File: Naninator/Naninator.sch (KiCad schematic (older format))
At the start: 25 parts, among them J1 CONN_02X03, J101 USB_OTG, J2 CONN_01X15, J3 CONN_01X15, U001 FT232RL, U201 MAX8881, U401 ATMEGA328P-M, Y406 16MHz

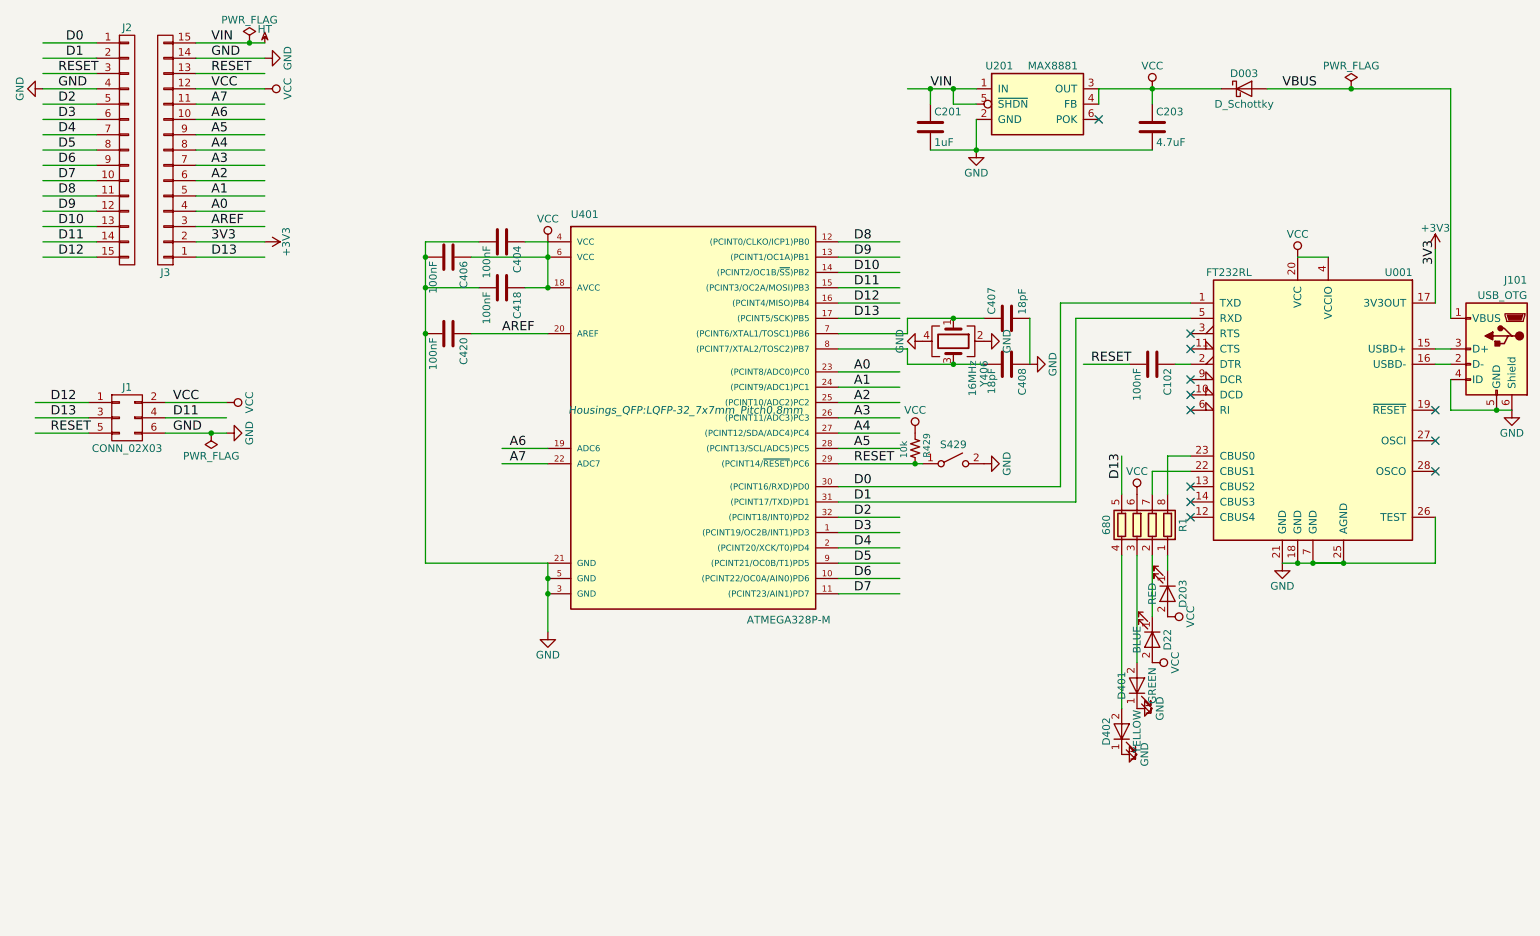
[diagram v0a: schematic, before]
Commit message: Routed the Naninator, except for two tracks
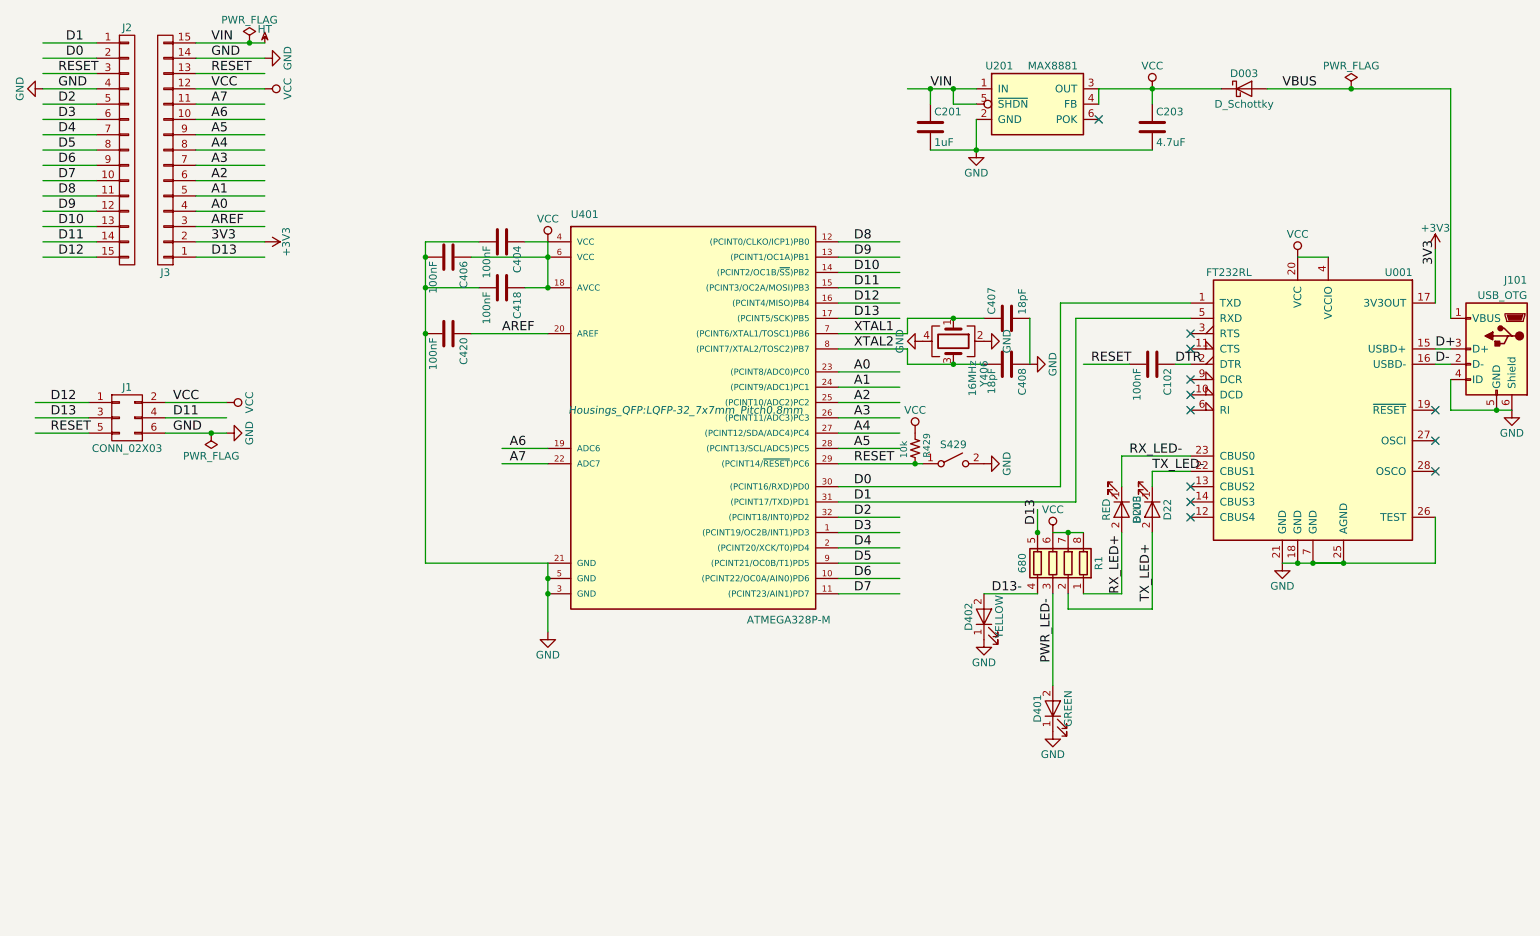
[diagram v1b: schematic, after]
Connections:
- net labels added: D+, D-, D13-, DTR, PWR_LED-, RX_LED+, RX_LED-, TX_LED+, TX_LED-, XTAL1, XTAL2
- wire segments 112 -> 116
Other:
- moved on the sheet: D203, D22, D401, D402, R1
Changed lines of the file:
@@
 $EndComp
+Wire Wire Line
+	1150 1050 800  1050
 Wire Wire Line
 	1150 950  800  950
 Wire Wire Line
-	1150 1050 800  1050
-Wire Wire Line
 	1150 1150 800  1150
 Wire Wire Line
 	1150 1250 800  1250
+Text Label 950  1050 0    60   ~ 0
+D0
 Text Label 950  950  0    60   ~ 0
-D0
-Text Label 950  1050 0    60   ~ 0
 D1
 Text Label 900  1150 0    60   ~ 0
@@
 L R_Pack04 R1
 U 1 1 58B740EE
-P 7950 4100
-F 0 "R1" V 7650 4100 50  0000 C CNN
-F 1 "680" V 8150 4100 50  0000 C CNN
-F 2 "Resistors_SMD:R_Array_Convex_4x0402" V 8225 4100 50  0001 C CNN
-F 3 "" H 7950 4100 50  0001 C CNN
-	1    7950 4100
+P 7400 4350
+F 0 "R1" V 7100 4350 50  0000 C CNN
+F 1 "680" V 7600 4350 50  0000 C CNN
+F 2 "Resistors_SMD:R_Array_Convex_4x0402" V 7675 4350 50  0001 C CNN
+F 3 "" H 7400 4350 50  0001 C CNN
+	1    7400 4350
 	-1   0    0    -1
 $EndComp
 Wire Wire Line
-	8300 3650 8150 3650
-Wire Wire Line
-	8150 3650 8150 3900
+	8300 3650 7850 3650
 Wire Wire Line
 	8300 3750 8050 3750
 Wire Wire Line
-	8050 3750 8050 3900
-Wire Wire Line
-	7850 3650 7850 3900
-Text Label 7850 3800 1    60   ~ 0
-D13
+	7300 4000 7300 4150
 $Comp
 L LED D203
 U 1 1 58B745FB
-P 8150 4550
-F 0 "D203" H 8150 4650 50  0000 C CNN
-F 1 "RED" H 8150 4450 50  0000 C CNN
-F 2 "LEDs:LED_0603" H 8150 4550 50  0001 C CNN
-F 3 "" H 8150 4550 50  0001 C CNN
-	1    8150 4550
+P 7850 4000
+F 0 "D203" H 7850 4100 50  0000 C CNN
+F 1 "RED" H 7850 3900 50  0000 C CNN
+F 2 "LEDs:LED_0603" H 7850 4000 50  0001 C CNN
+F 3 "" H 7850 4000 50  0001 C CNN
+	1    7850 4000
 	0    1    1    0
 $EndComp
@@
 L LED D22
 U 1 1 58B746B4
-P 8050 4850
-F 0 "D22" H 8050 4950 50  0000 C CNN
-F 1 "BLUE" H 8050 4750 50  0000 C CNN
-F 2 "LEDs:LED_0603" H 8050 4850 50  0001 C CNN
-F 3 "" H 8050 4850 50  0001 C CNN
-	1    8050 4850
+P 8050 4000
+F 0 "D22" H 8050 4100 50  0000 C CNN
+F 1 "BLUE" H 8050 3900 50  0000 C CNN
+F 2 "LEDs:LED_0603" H 8050 4000 50  0001 C CNN
+F 3 "" H 8050 4000 50  0001 C CNN
+	1    8050 4000
 	0    1    1    0
 $EndComp
@@
 L LED D401
 U 1 1 58B74705
-P 7950 5150
-F 0 "D401" H 7950 5250 50  0000 C CNN
-F 1 "GREEN" H 7950 5050 50  0000 C CNN
-F 2 "LEDs:LED_0603" H 7950 5150 50  0001 C CNN
-F 3 "" H 7950 5150 50  0001 C CNN
-	1    7950 5150
+P 7400 5300
+F 0 "D401" H 7400 5400 50  0000 C CNN
+F 1 "GREEN" H 7400 5200 50  0000 C CNN
+F 2 "LEDs:LED_0603" H 7400 5300 50  0001 C CNN
+F 3 "" H 7400 5300 50  0001 C CNN
+	1    7400 5300
 	0    -1   -1   0
 $EndComp
@@
 L LED D402
 U 1 1 58B74757
-P 7850 5450
-F 0 "D402" H 7850 5550 50  0000 C CNN
-F 1 "YELLOW" H 7850 5350 50  0000 C CNN
-F 2 "LEDs:LED_0603" H 7850 5450 50  0001 C CNN
-F 3 "" H 7850 5450 50  0001 C CNN
-	1    7850 5450
+P 6950 4700
+F 0 "D402" H 6950 4800 50  0000 C CNN
+F 1 "YELLOW" H 6950 4600 50  0000 C CNN
+F 2 "LEDs:LED_0603" H 6950 4700 50  0001 C CNN
+F 3 "" H 6950 4700 50  0001 C CNN
+	1    6950 4700
 	0    -1   -1   0
 $EndComp
 Wire Wire Line
-	8150 4400 8150 4300
-Wire Wire Line
-	8050 4700 8050 4300
-Wire Wire Line
-	7950 5000 7950 4300
-Wire Wire Line
-	7850 5300 7850 4300
+	7400 5150 7400 4550
+Wire Wire Line
+	6950 4550 7300 4550
 $Comp
 L VCC #PWR09
 U 1 1 58B74D0E
-P 7950 3900
-F 0 "#PWR09" H 7950 3750 50  0001 C CNN
-F 1 "VCC" H 7950 4050 50  0000 C CNN
-F 2 "" H 7950 3900 50  0001 C CNN
-F 3 "" H 7950 3900 50  0001 C CNN
-	1    7950 3900
-	1    0    0    -1
-$EndComp
-$Comp
-L VCC #PWR010
-U 1 1 58B74D48
-P 8150 4700
-F 0 "#PWR010" H 8150 4550 50  0001 C CNN
-F 1 "VCC" H 8150 4850 50  0000 C CNN
-F 2 "" H 8150 4700 50  0001 C CNN
-F 3 "" H 8150 4700 50  0001 C CNN
-	1    8150 4700
-	0    1    1    0
-$EndComp
-$Comp
-L VCC #PWR011
-U 1 1 58B74D82
-P 8050 5000
-F 0 "#PWR011" H 8050 4850 50  0001 C CNN
-F 1 "VCC" H 8050 5150 50  0000 C CNN
-F 2 "" H 8050 5000 50  0001 C CNN
-F 3 "" H 8050 5000 50  0001 C CNN
-	1    8050 5000
-	0    1    1    0
-$EndComp
-$Comp
-L GND #PWR012
+P 7400 4150
+F 0 "#PWR09" H 7400 4000 50  0001 C CNN
+F 1 "VCC" H 7400 4300 50  0000 C CNN
+F 2 "" H 7400 4150 50  0001 C CNN
+F 3 "" H 7400 4150 50  0001 C CNN
+	1    7400 4150
+	1    0    0    -1
+$EndComp
+$Comp
+L GND #PWR010
 U 1 1 58B74DBC
-P 7950 5300
-F 0 "#PWR012" H 7950 5050 50  0001 C CNN
-F 1 "GND" H 7950 5150 50  0000 C CNN
-F 2 "" H 7950 5300 50  0001 C CNN
-F 3 "" H 7950 5300 50  0001 C CNN
-	1    7950 5300
-	0    -1   -1   0
-$EndComp
-$Comp
-L GND #PWR013
+P 7400 5450
+F 0 "#PWR010" H 7400 5200 50  0001 C CNN
+F 1 "GND" H 7400 5300 50  0000 C CNN
+F 2 "" H 7400 5450 50  0001 C CNN
+F 3 "" H 7400 5450 50  0001 C CNN
+	1    7400 5450
+	1    0    0    -1
+$EndComp
+$Comp
+L GND #PWR011
 U 1 1 58B74DF6
-P 7850 5600
-F 0 "#PWR013" H 7850 5350 50  0001 C CNN
-F 1 "GND" H 7850 5450 50  0000 C CNN
-F 2 "" H 7850 5600 50  0001 C CNN
-F 3 "" H 7850 5600 50  0001 C CNN
-	1    7850 5600
-	0    -1   -1   0
+P 6950 4850
+F 0 "#PWR011" H 6950 4600 50  0001 C CNN
+F 1 "GND" H 6950 4700 50  0000 C CNN
+F 2 "" H 6950 4850 50  0001 C CNN
+F 3 "" H 6950 4850 50  0001 C CNN
+	1    6950 4850
+	1    0    0    -1
 $EndComp
 $Comp
@@
 $EndComp
 $Comp
-L HT #PWR014
+L HT #PWR012
 U 1 1 58B73E40
 P 2250 950
-F 0 "#PWR014" H 2250 1070 50  0001 C CNN
+F 0 "#PWR012" H 2250 1070 50  0001 C CNN
 F 1 "HT" H 2250 1040 50  0000 C CNN
 F 2 "" H 2250 950 50  0001 C CNN
@@
 Connection ~ 6750 1250
 $Comp
-L GND #PWR015
+L GND #PWR013
 U 1 1 58B74079
 P 6900 1650
-F 0 "#PWR015" H 6900 1400 50  0001 C CNN
+F 0 "#PWR013" H 6900 1400 50  0001 C CNN
 F 1 "GND" H 6900 1500 50  0000 C CNN
 F 2 "" H 6900 1650 50  0001 C CNN
@@
 3V3
 $Comp
-L +3V3 #PWR016
+L +3V3 #PWR014
 U 1 1 58B7578F
 P 9900 2300
-F 0 "#PWR016" H 9900 2150 50  0001 C CNN
+F 0 "#PWR014" H 9900 2150 50  0001 C CNN
 F 1 "+3V3" H 9900 2440 50  0000 C CNN
 F 2 "" H 9900 2300 50  0001 C CNN
@@
 $EndComp
 $Comp
-L GND #PWR017
+L GND #PWR015
 U 1 1 58B75EDB
 P 10400 3350
-F 0 "#PWR017" H 10400 3100 50  0001 C CNN
+F 0 "#PWR015" H 10400 3100 50  0001 C CNN
 F 1 "GND" H 10400 3200 50  0000 C CNN
 F 2 "" H 10400 3350 50  0001 C CNN
@@
 $EndComp
 $Comp
-L +3V3 #PWR018
+L +3V3 #PWR016
 U 1 1 58B75F1F
 P 2250 2250
-F 0 "#PWR018" H 2250 2100 50  0001 C CNN
+F 0 "#PWR016" H 2250 2100 50  0001 C CNN
 F 1 "+3V3" H 2250 2390 50  0000 C CNN
 F 2 "" H 2250 2250 50  0001 C CNN
@@
 $EndComp
 $Comp
-L VCC #PWR019
+L VCC #PWR017
 U 1 1 58B75F63
 P 9000 2350
-F 0 "#PWR019" H 9000 2200 50  0001 C CNN
+F 0 "#PWR017" H 9000 2200 50  0001 C CNN
 F 1 "VCC" H 9000 2500 50  0000 C CNN
 F 2 "" H 9000 2350 50  0001 C CNN
@@
 Connection ~ 9100 4350
 $Comp
-L GND #PWR020
+L GND #PWR018
 U 1 1 58B76440
 P 8900 4350
-F 0 "#PWR020" H 8900 4100 50  0001 C CNN
+F 0 "#PWR018" H 8900 4100 50  0001 C CNN
 F 1 "GND" H 8900 4200 50  0000 C CNN
 F 2 "" H 8900 4350 50  0001 C CNN
@@
 NoConn ~ 7700 1450
 $Comp
-L PWR_FLAG #FLG021
+L PWR_FLAG #FLG019
 U 1 1 58B8A8A6
 P 2150 950
-F 0 "#FLG021" H 2150 1025 50  0001 C CNN
+F 0 "#FLG019" H 2150 1025 50  0001 C CNN
 F 1 "PWR_FLAG" H 2150 1100 50  0000 C CNN
 F 2 "" H 2150 950 50  0001 C CNN
@@
 $EndComp
 $Comp
-L PWR_FLAG #FLG022
+L PWR_FLAG #FLG020
 U 1 1 58B8A8E8
 P 1900 3500
-F 0 "#FLG022" H 1900 3575 50  0001 C CNN
+F 0 "#FLG020" H 1900 3575 50  0001 C CNN
 F 1 "PWR_FLAG" H 1900 3650 50  0000 C CNN
 F 2 "" H 1900 3500 50  0001 C CNN
@@
 $EndComp
 $Comp
-L VCC #PWR023
+L VCC #PWR021
 U 1 1 58B8B4A6
 P 8050 1250
-F 0 "#PWR023" H 8050 1100 50  0001 C CNN
+F 0 "#PWR021" H 8050 1100 50  0001 C CNN
 F 1 "VCC" H 8050 1400 50  0000 C CNN
 F 2 "" H 8050 1250 50  0001 C CNN
@@
 Connection ~ 2150 950
 $Comp
-L GND #PWR024
+L GND #PWR022
 U 1 1 58B8C7FC
 P 6950 3700
-F 0 "#PWR024" H 6950 3450 50  0001 C CNN
+F 0 "#PWR022" H 6950 3450 50  0001 C CNN
 F 1 "GND" H 6950 3550 50  0000 C CNN
 F 2 "" H 6950 3700 50  0001 C CNN
@@
 Connection ~ 6500 3700
 $Comp
-L VCC #PWR025
+L VCC #PWR023
 U 1 1 58B8D268
 P 6500 3500
-F 0 "#PWR025" H 6500 3350 50  0001 C CNN
+F 0 "#PWR023" H 6500 3350 50  0001 C CNN
 F 1 "VCC" H 6500 3650 50  0000 C CNN
 F 2 "" H 6500 3500 50  0001 C CNN
@@
 VBUS
 $Comp
-L PWR_FLAG #FLG026
+L PWR_FLAG #FLG024
 U 1 1 58B8D917
 P 9350 1250
-F 0 "#FLG026" H 9350 1325 50  0001 C CNN
+F 0 "#FLG024" H 9350 1325 50  0001 C CNN
 F 1 "PWR_FLAG" H 9350 1400 50  0000 C CNN
 F 2 "" H 9350 1250 50  0001 C CNN
@@
 $EndComp
 $Comp
-L GND #PWR027
+L GND #PWR025
 U 1 1 58BA02E7
 P 6950 2900
-F 0 "#PWR027" H 6950 2650 50  0001 C CNN
+F 0 "#PWR025" H 6950 2650 50  0001 C CNN
 F 1 "GND" H 6950 2750 50  0000 C CNN
 F 2 "" H 6950 2900 50  0001 C CNN
@@
 	0    -1   -1   0
 $EndComp
-$Comp
-L GND #PWR028
-U 1 1 58BA032D
+Wire Wire Line
+	7850 3650 7850 3850
+Wire Wire Line
+	8050 3750 8050 3850
+Wire Wire Line
+	7400 4150 7600 4150
+Wire Wire Line
+	8050 4150 8050 4650
+Wire Wire Line
+	8050 4650 7500 4650
+Wire Wire Line
+	7500 4650 7500 4550
+Wire Wire Line
+	7850 4150 7850 4550
+Wire Wire Line
+	7850 4550 7600 4550
+Text Label 7300 4100 1    60   ~ 0
+D13
+Connection ~ 7300 4150
+Text Label 9900 2950 0    60   ~ 0
+D+
+Text Label 9900 3050 0    60   ~ 0
+D-
+Text Label 7900 3650 0    60   ~ 0
+RX_LED-
+Text Label 8050 3750 0    60   ~ 0
+TX_LED-
+Text Label 7850 4550 1    60   ~ 0
+RX_LED+
+Text Label 8050 4600 1    60   ~ 0
+TX_LED+
+Text Label 8200 3050 0    60   ~ 0
+DTR
+Text Label 6100 2850 0    60   ~ 0
+XTAL1
+Text Label 6100 2950 0    60   ~ 0
+XTAL2
+Connection ~ 7500 4150
+Text Label 7000 4550 0    60   ~ 0
+D13-
+Text Label 7400 5000 1    60   ~ 0
+PWR_LED-
+$Comp
+L GND #PWR?
+U 1 1 58BC5FE1
 P 6550 2900
-F 0 "#PWR028" H 6550 2650 50  0001 C CNN
+F 0 "#PWR?" H 6550 2650 50  0001 C CNN
 F 1 "GND" H 6550 2750 50  0000 C CNN
 F 2 "" H 6550 2900 50  0001 C CNN

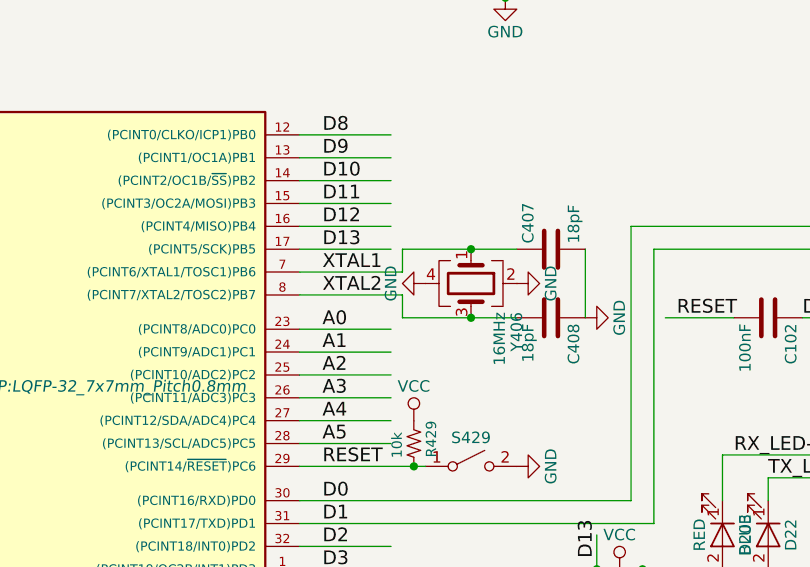
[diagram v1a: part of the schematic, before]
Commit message: One or two ground connections are left
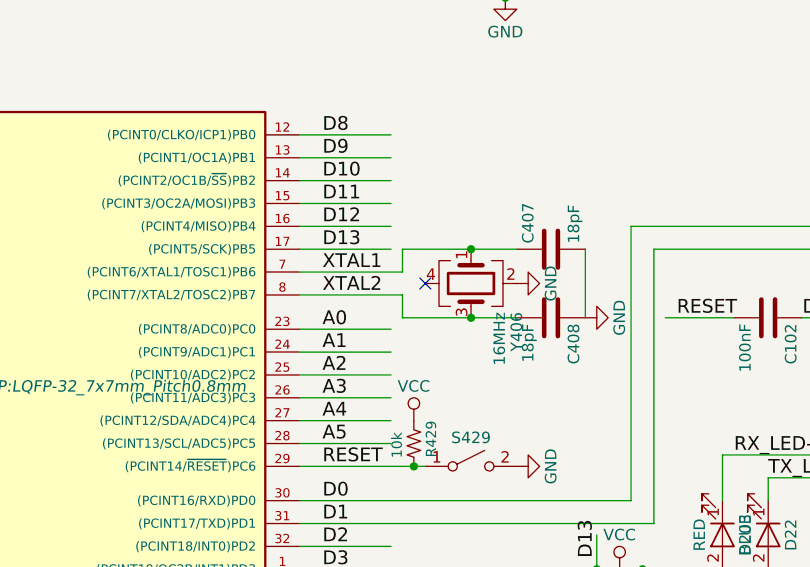
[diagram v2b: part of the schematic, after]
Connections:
- no-connect marks 12 -> 13
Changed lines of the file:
@@
 Text Label 7400 5000 1    60   ~ 0
 PWR_LED-
-$Comp
-L GND #PWR?
-U 1 1 58BC5FE1
-P 6550 2900
-F 0 "#PWR?" H 6550 2650 50  0001 C CNN
-F 1 "GND" H 6550 2750 50  0000 C CNN
-F 2 "" H 6550 2900 50  0001 C CNN
-F 3 "" H 6550 2900 50  0001 C CNN
-	1    6550 2900
-	0    1    1    0
-$EndComp
+NoConn ~ 6550 2900
 $EndSCHEMATC

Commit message: Consistentized the Naninator, Tomo, and Tomo Plugin
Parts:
- removed C404, C406, C418, C420: 100nF, Capacitors_SMD:C_0402_NoSilk, symbol C
- removed C407, C408: 18pF, Capacitors_SMD:C_0402_NoSilk, symbol C
- removed J101: USB_OTG, Connectors_Molex:USB_Micro-B_Molex_47346-0001, symbol USB_OTG
- removed R429: 10k, Resistors_SMD:R_0402_NoSilk, symbol RESISTOR
- removed S429: SW_SPST, Buttons_Switches_SMD:SW_SPST_B3U-1000P, symbol SW_SPST
- removed U401: ATMEGA328P-M, Housings_QFP:LQFP-32_7x7mm_Pitch0.8mm, symbol ATMEGA328P-M
- removed Y406: 16MHz, Crystals:Crystal_SMD_2520-4pin_2.5x2.0mm, symbol Crystal_GND24
- added J101: USB_MICROB, Connectors_Molex:USB_Micro-B_Molex_47346-0001, symbol USB_MICROB
- D003: value D_Schottky -> MSSP12L; Digikey (none) -> MSS1P2L-M3/89AIGICT-ND
- D022: renamed from D22; footprint LEDs:LED_0603 -> KwanSystems:D_0603
- D023: renamed from D203; footprint LEDs:LED_0603 -> KwanSystems:D_0603
- D401, D402: footprint LEDs:LED_0603 -> KwanSystems:D_0603
- U201: value MAX8881 -> MAX8881 5V
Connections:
- net labels added: +5V, D0/RX, D1/TX
- net labels removed: D0, D1, XTAL1, XTAL2
- wire segments 116 -> 98
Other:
- note added: "CBUS0 has function #TXLED\nby default, but this is from the\npoint of view of the FT232/Host,\nso it is RX_LED from the point\nof view of this device. Vice versa\nfor CBUS1"
- note added: "Note that RX and TX are\ncrossed over because FT232\nis labeled from point of view\nof USB Host"
- moved on the sheet: C102, D022, D023, D401, D402, R1, U001

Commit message: j
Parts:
- removed C102: 100nF, Capacitors_SMD:C_0402_NoSilk, symbol C
- removed D022: BLUE, KwanSystems:D_0603, symbol LED
- removed D023: RED, KwanSystems:D_0603, symbol LED
- removed J101: USB_MICROB, Connectors_Molex:USB_Micro-B_Molex_47346-0001, symbol USB_MICROB
- removed R1: 680, Resistors_SMD:R_Array_Convex_4x0402, symbol R_Pack04
- removed U001: FT232RL, Housings_SSOP:SSOP-28_5.3x10.2mm_Pitch0.65mm, symbol FT232RL
- added G101: Designed With, KwanSystems:Symbol_KiCAD-Logo_CopperAndSilkScreenTop_small, symbol KwanSystems:DesignedWithKicad
- added G102: KwanSystems, KwanSystems:StKwansSoldermask, symbol KwanSystems:KwanSystems
- added R201: 680, KwanSystems:R_Array_Convex_4x0402, symbol KwanSystems:RP4
- C201, C203: footprint Capacitors_SMD:C_0402_NoSilk -> Capacitor_SMD:C_0402_1005Metric; symbol C -> Device:C_Small
- D3: renamed from D003; footprint KwanSystems:MicroSMP -> Diode_SMD:D_TUMD2; symbol D_Schottky -> Device:D_Schottky
- D401, D402: symbol LED -> Naninator-rescue:LED
- J1: footprint Pin_Headers:Pin_Header_Straight_2x03_Pitch2.54mm -> Connector_PinHeader_2.54mm:PinHeader_2x03_P2.54mm_Vertical; symbol CONN_02X03 -> Connector_Generic:Conn_02x03_Odd_Even
- J2, J3: footprint Pin_Headers:Pin_Header_Straight_1x15_Pitch2.54mm -> Connector_PinHeader_2.54mm:PinHeader_1x15_P2.54mm_Vertical; symbol CONN_01X15 -> Connector_Generic:Conn_01x15
- U201: symbol MAX8881 -> Naninator-rescue:MAX8881
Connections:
- net labels added: ~RESET
- net labels removed: +5V, 3V3, D+, D-, DTR, RESET, RX_LED+, RX_LED-, TX_LED+, TX_LED-
- wire segments 98 -> 84
- no-connect marks 13 -> 1
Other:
- note added: "3V3 is powered from FT232 regulator. Cypress\nCY7C65213 is mostly pin-compatible but doesn't\nhave an exposed regulator, so this pin won't work\nwith it."
- note removed: "CBUS0 has function #TXLED\nby default, but this is from the\npoint of view of the FT232/Host,\nso it is RX_LED from the point\nof view of this device. Vice versa\nfor CBUS1"
- moved on the sheet: D401, D402
